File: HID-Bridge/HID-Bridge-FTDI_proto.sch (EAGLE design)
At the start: 7 parts, among them U1 FT232RLSSOP

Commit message: Changes for sides etc.
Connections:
- net N$1: now also U1.RXD; no longer U1.TXD
- net N$4: now also U1.TXD; no longer U1.RXD
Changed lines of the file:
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@@
 <net name="N$1" class="0">
 <segment>
-<pinref part="U1" gate="G$1" pin="TXD"/>
-<wire x1="121.92" y1="101.6" x2="132.08" y2="101.6" width="0.1524" layer="91"/>
-<wire x1="132.08" y1="101.6" x2="132.08" y2="86.36" width="0.1524" layer="91"/>
 <pinref part="JP2" gate="G$1" pin="2"/>
-<wire x1="132.08" y1="86.36" x2="137.16" y2="86.36" width="0.1524" layer="91"/>
+<wire x1="137.16" y1="86.36" x2="124.46" y2="86.36" width="0.1524" layer="91"/>
+<wire x1="124.46" y1="86.36" x2="124.46" y2="99.06" width="0.1524" layer="91"/>
+<pinref part="U1" gate="G$1" pin="RXD"/>
+<wire x1="124.46" y1="99.06" x2="121.92" y2="99.06" width="0.1524" layer="91"/>
 </segment>
 </net>
 <net name="N$4" class="0">
 <segment>
-<pinref part="U1" gate="G$1" pin="RXD"/>
-<wire x1="121.92" y1="99.06" x2="129.54" y2="99.06" width="0.1524" layer="91"/>
-<wire x1="129.54" y1="99.06" x2="129.54" y2="83.82" width="0.1524" layer="91"/>
+<pinref part="U1" gate="G$1" pin="TXD"/>
+<wire x1="121.92" y1="101.6" x2="127" y2="101.6" width="0.1524" layer="91"/>
+<wire x1="127" y1="101.6" x2="127" y2="83.82" width="0.1524" layer="91"/>
 <pinref part="JP2" gate="G$1" pin="3"/>
-<wire x1="129.54" y1="83.82" x2="137.16" y2="83.82" width="0.1524" layer="91"/>
+<wire x1="127" y1="83.82" x2="137.16" y2="83.82" width="0.1524" layer="91"/>
 </segment>
 </net>

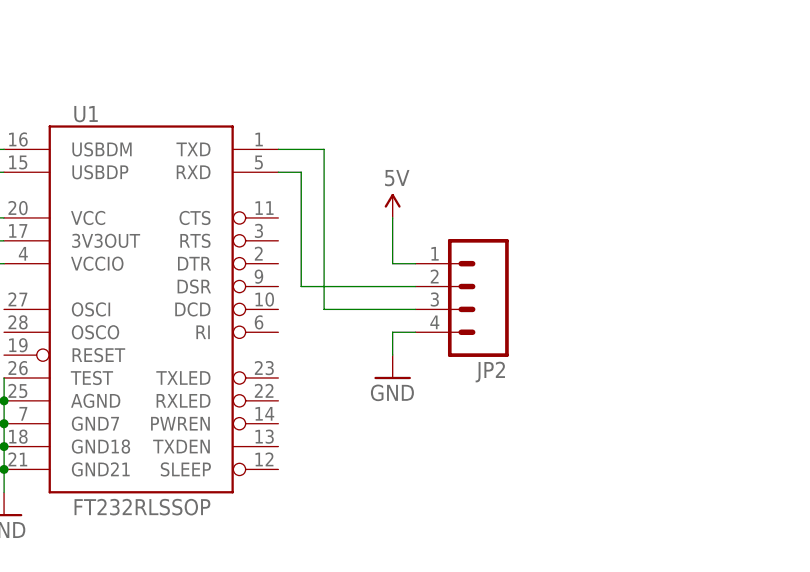
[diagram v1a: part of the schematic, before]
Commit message: Changes on FTDI, larger clearance &c
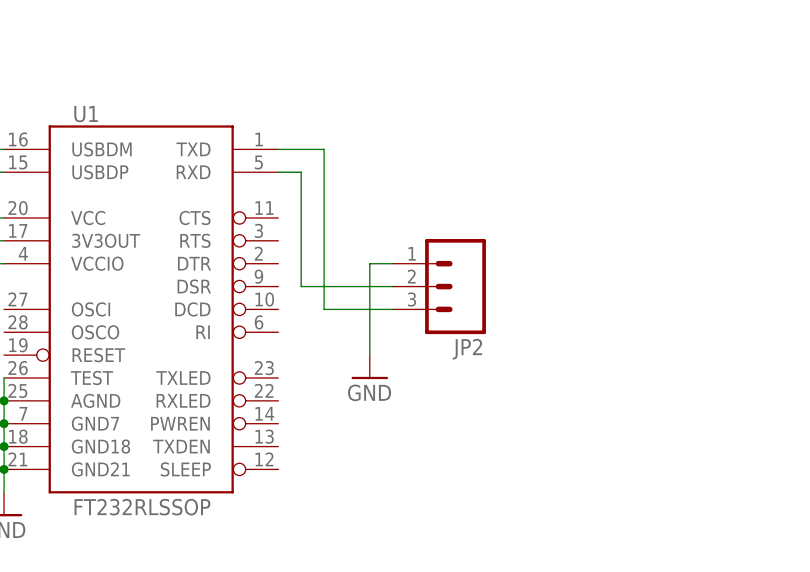
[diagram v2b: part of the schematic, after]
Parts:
- JP2: device SparkFun-Connectors:M04PTH -> SparkFun-Connectors:M03PTH
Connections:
- net 5V: no longer JP2.1
- net GND: now also JP2.1; no longer JP2.4
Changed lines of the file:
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@@
 <part name="GND6" library="SparkFun-Aesthetics" deviceset="GND" device=""/>
 <part name="SUPPLY3" library="SparkFun-Aesthetics" deviceset="5V" device=""/>
-<part name="JP2" library="SparkFun-Connectors" deviceset="M04" device="PTH"/>
-<part name="SUPPLY4" library="SparkFun-Aesthetics" deviceset="5V" device=""/>
+<part name="JP2" library="SparkFun-Connectors" deviceset="M03" device="PTH"/>
 <part name="GND2" library="SparkFun-Aesthetics" deviceset="GND" device=""/>
 </parts>
@@
 <instance part="SUPPLY3" gate="G$1" x="81.28" y="109.22"/>
 <instance part="JP2" gate="G$1" x="142.24" y="86.36" rot="R180"/>
-<instance part="SUPPLY4" gate="G$1" x="134.62" y="93.98"/>
-<instance part="GND2" gate="1" x="134.62" y="76.2"/>
+<instance part="GND2" gate="1" x="132.08" y="76.2"/>
 </instances>
 <busses>
@@
 </segment>
 <segment>
-<pinref part="JP2" gate="G$1" pin="4"/>
 <pinref part="GND2" gate="1" pin="GND"/>
-<wire x1="137.16" y1="81.28" x2="134.62" y2="81.28" width="0.1524" layer="91"/>
-<wire x1="134.62" y1="81.28" x2="134.62" y2="78.74" width="0.1524" layer="91"/>
+<wire x1="132.08" y1="78.74" x2="132.08" y2="88.9" width="0.1524" layer="91"/>
+<pinref part="JP2" gate="G$1" pin="1"/>
+<wire x1="132.08" y1="88.9" x2="134.62" y2="88.9" width="0.1524" layer="91"/>
 </segment>
 </net>
@@
 <wire x1="81.28" y1="88.9" x2="81.28" y2="109.22" width="0.1524" layer="91"/>
 </segment>
-<segment>
-<pinref part="JP2" gate="G$1" pin="1"/>
-<pinref part="SUPPLY4" gate="G$1" pin="5V"/>
-<wire x1="137.16" y1="88.9" x2="134.62" y2="88.9" width="0.1524" layer="91"/>
-<wire x1="134.62" y1="88.9" x2="134.62" y2="93.98" width="0.1524" layer="91"/>
-</segment>
 </net>
 <net name="3.3V" class="0">
@@
 <segment>
 <pinref part="JP2" gate="G$1" pin="2"/>
-<wire x1="137.16" y1="86.36" x2="124.46" y2="86.36" width="0.1524" layer="91"/>
+<wire x1="134.62" y1="86.36" x2="124.46" y2="86.36" width="0.1524" layer="91"/>
 <wire x1="124.46" y1="86.36" x2="124.46" y2="99.06" width="0.1524" layer="91"/>
 <pinref part="U1" gate="G$1" pin="RXD"/>
@@
 <wire x1="127" y1="101.6" x2="127" y2="83.82" width="0.1524" layer="91"/>
 <pinref part="JP2" gate="G$1" pin="3"/>
-<wire x1="127" y1="83.82" x2="137.16" y2="83.82" width="0.1524" layer="91"/>
+<wire x1="127" y1="83.82" x2="134.62" y2="83.82" width="0.1524" layer="91"/>
 </segment>
 </net>
